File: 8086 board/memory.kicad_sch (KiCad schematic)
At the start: 43 parts, among them U10 74AC573, U11 74HC138, U12 74HC138, U13 IS61C6416AL, U3 74HC14, U39 29F800BA, U40 IS61C6416AL, U8 74AC573, U9 74AC573

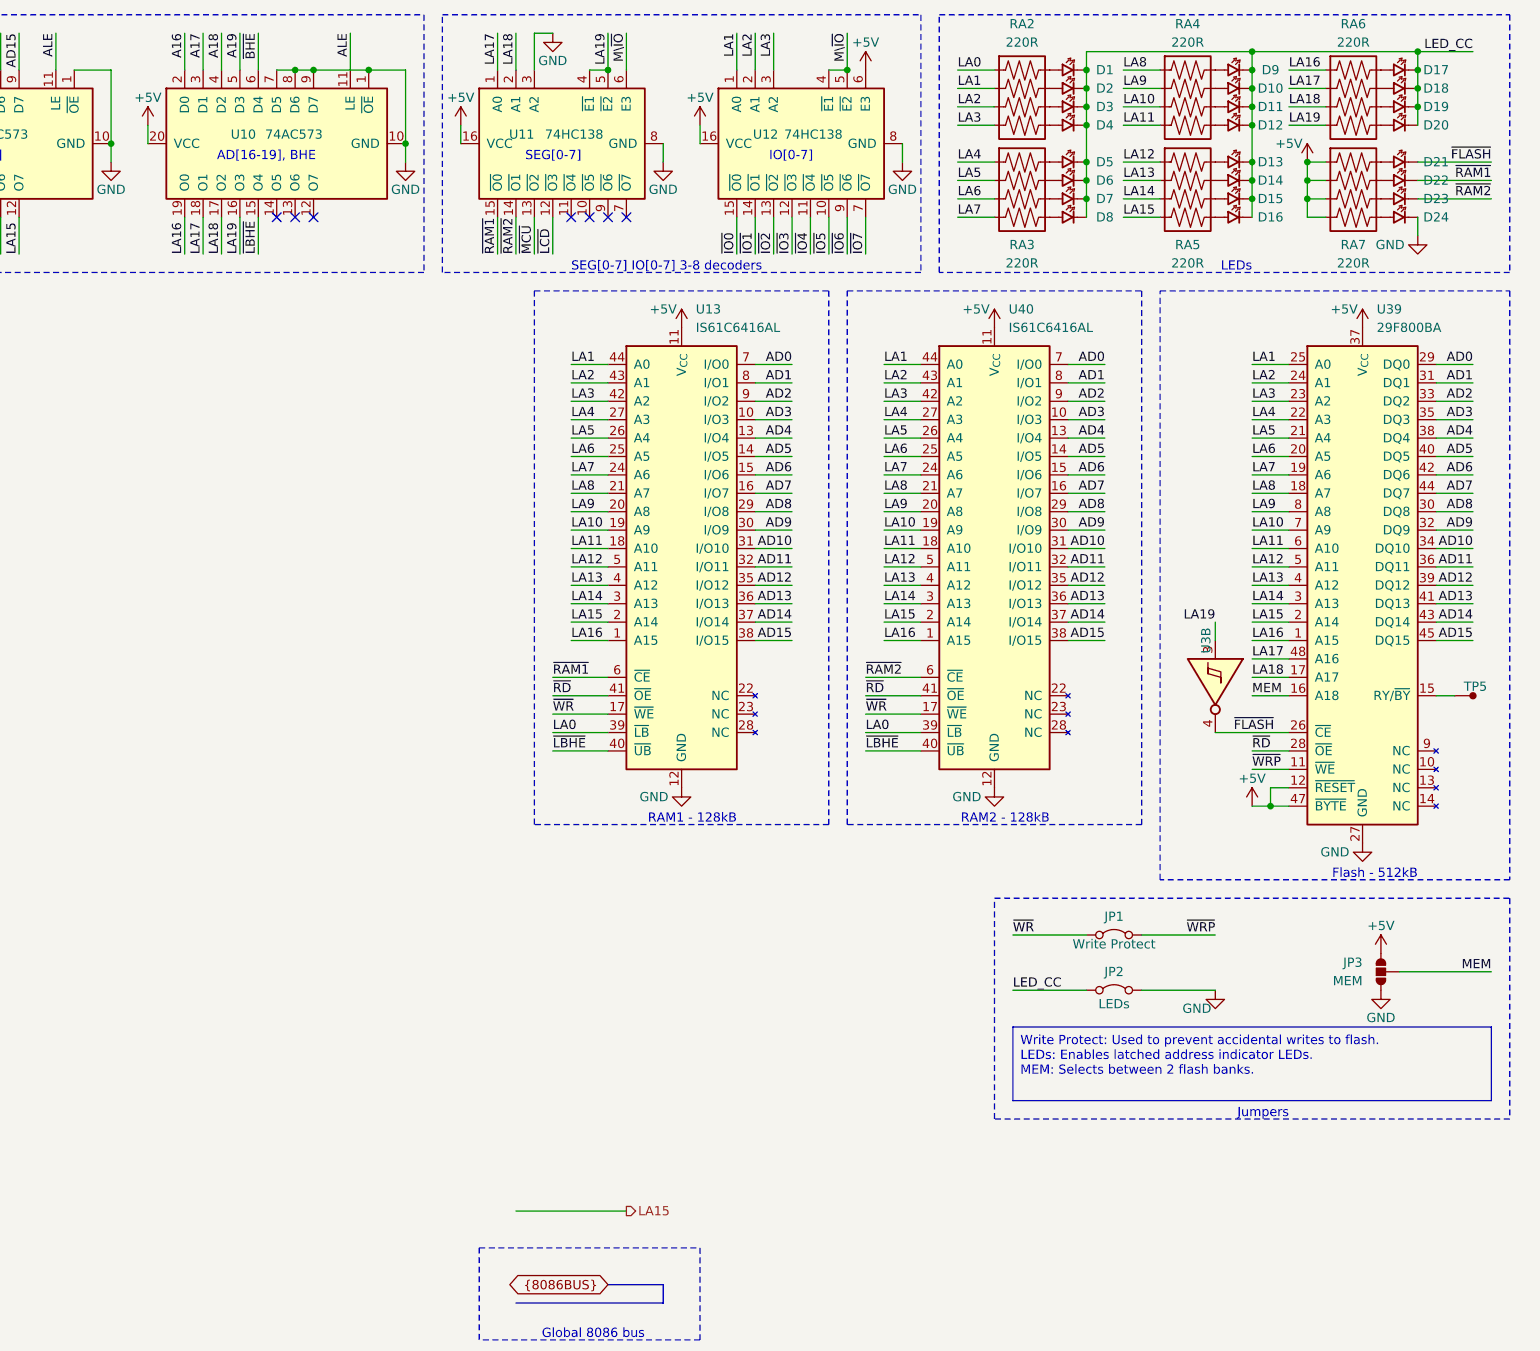
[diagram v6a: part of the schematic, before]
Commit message: reduced schematic, PCB memory routed
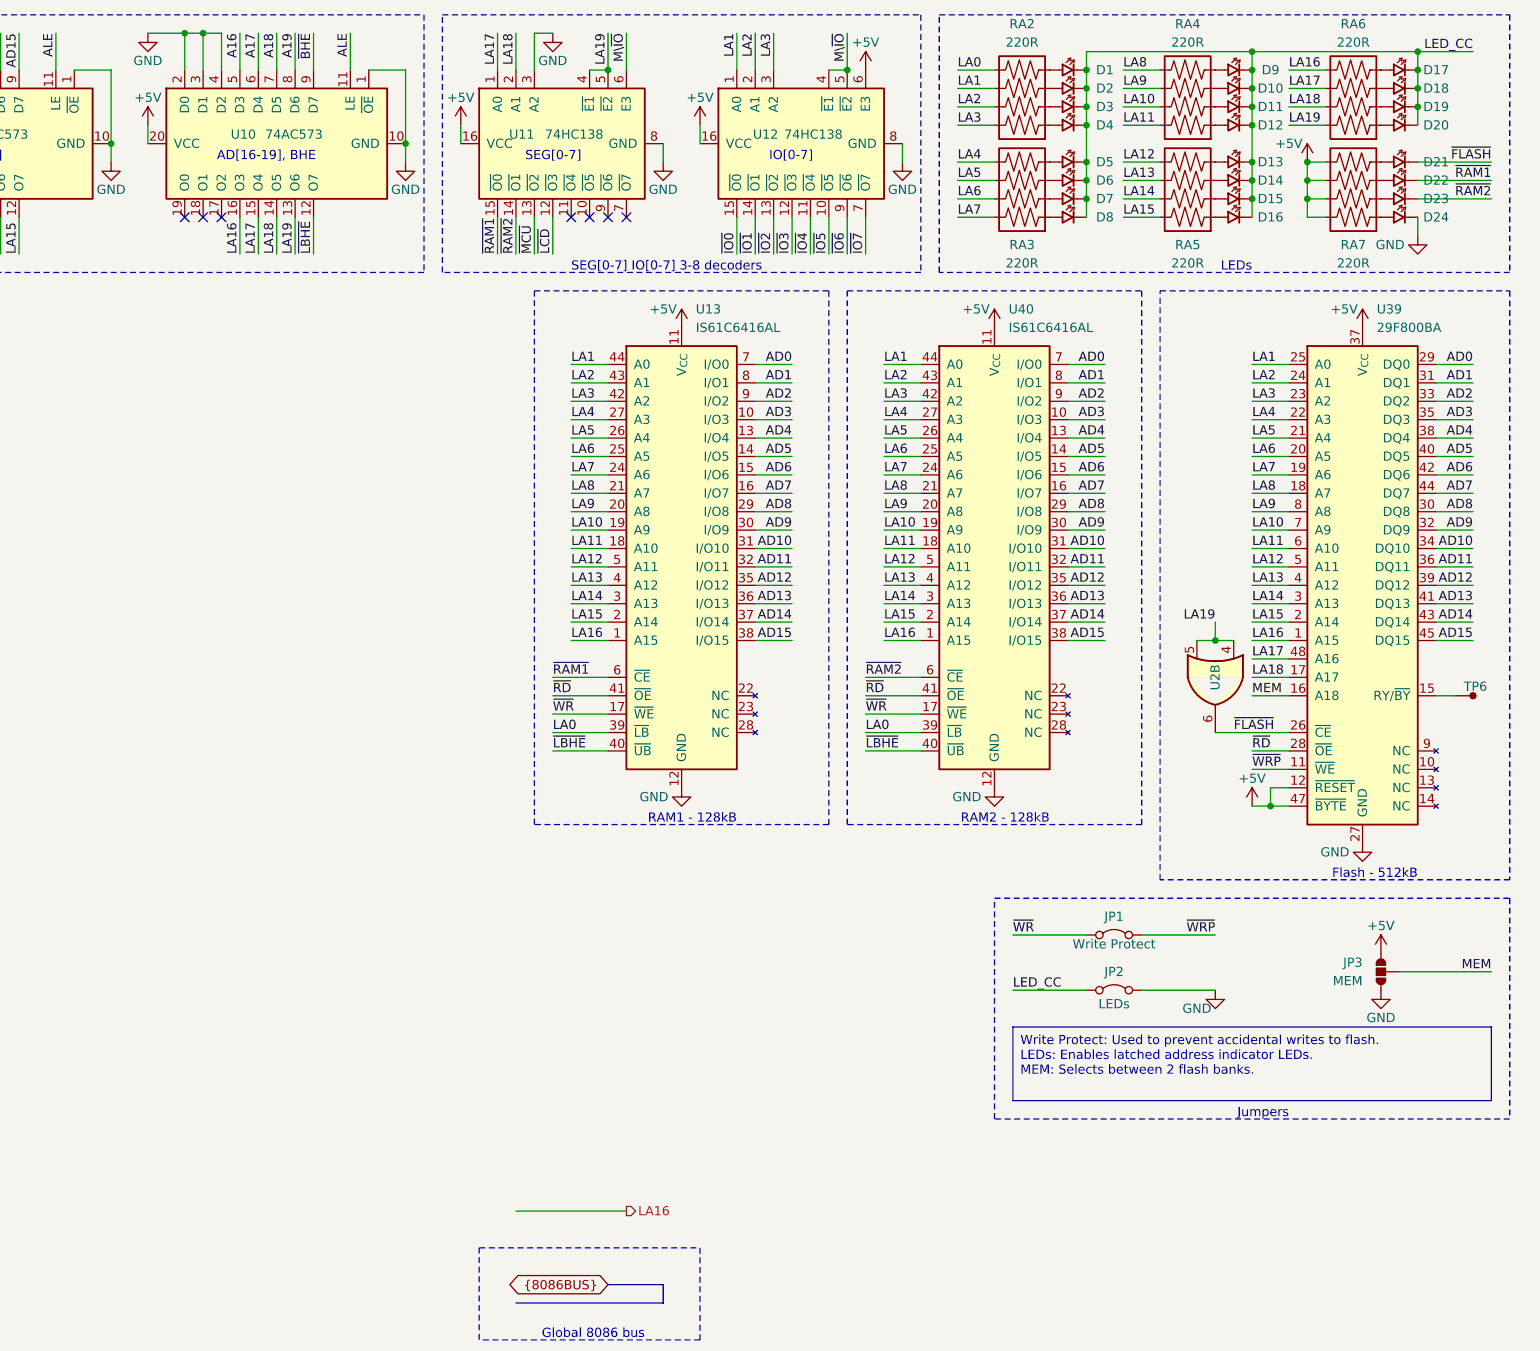
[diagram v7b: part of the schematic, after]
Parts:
- removed U3: 74HC14, Package_SO:SOIC-14_3.9x8.7mm_P1.27mm, symbol 8086PC:74HC14
- added U2: 74HC32, Package_SO:TSSOP-14_4.4x5mm_P0.65mm, symbol 8086PC:74HC32
- D21: value PWR -> FLASH
- D22: value ~{BHE} -> RAM1
- D23: value SEG0 -> RAM2
- D24: value SEG1 -> POWER
- TP6: renamed from TP5; footprint (none) -> TestPoint:TestPoint_Pad_1.5x1.5mm
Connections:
- net +5V: now also JP3.3, RA7.5, RA7.6, RA7.7, RA7.8; no longer JP3.2, RA7.1, RA7.2, RA7.3, RA7.4
- net A16: now also U10.5 (D3); no longer U10.2 (D0)
- net A17: now also U10.6 (D4); no longer U10.3 (D1)
- net A18: now also U10.7 (D5); no longer U10.4 (D2)
- net A19: now also U10.8 (D6); no longer U10.5 (D3)
- net GND: now also U10.2 (D0), U10.3 (D1), U10.4 (D2); no longer U10.7 (D5), U10.8 (D6), U10.9 (D7)
- net LA0: now also RA2.5; no longer RA2.1
- net LA1: now also RA2.6; no longer RA2.2
- net LA10: now also RA4.7; no longer RA4.3
- net LA11: now also RA4.8; no longer RA4.4
- net LA12: now also RA5.5; no longer RA5.1
- net LA13: now also RA5.6; no longer RA5.2
- net LA14: now also RA5.7; no longer RA5.3
- net LA15: now also RA5.8; no longer RA5.4
- net LA16: now also RA6.5, U10.16 (O3); no longer RA6.1, U10.19 (O0)
- net LA17: now also RA6.6, U10.15 (O4); no longer RA6.2, U10.18 (O1)
- net LA18: now also RA6.7, U10.14 (O5); no longer RA6.3, U10.17 (O2)
- net LA19: now also RA6.8, U10.13 (O6), U2.4, U2.5; no longer RA6.4, U10.16 (O3)
- net LA2: now also RA2.7; no longer RA2.3
- net LA3: now also RA2.8; no longer RA2.4
- net LA4: now also RA3.5; no longer RA3.1
- net LA5: now also RA3.6; no longer RA3.2
- net LA6: now also RA3.7; no longer RA3.3
- net LA7: now also RA3.8; no longer RA3.4
- net LA8: now also RA4.5; no longer RA4.1
- net LA9: now also RA4.6; no longer RA4.2
- net MEM: now also JP3.2; no longer JP3.3
- net ~{BHE}: now also U10.9 (D7); no longer U10.6 (D4)
- net ~{FLASH}: now also U2.6
- net ~{LBHE}: now also U10.12 (O7); no longer U10.15 (O4)
- net at D4.1 (A): now also RA2.1; no longer RA2.5
- net at D3.1 (A): now also RA2.2; no longer RA2.6
- net at D2.1 (A): now also RA2.3; no longer RA2.7
- net at D1.1 (A): now also RA2.4; no longer RA2.8
- net at D19.1 (A): now also RA6.2; no longer RA6.6
- net at D23.1 (A): now also RA7.2; no longer RA7.6
- net at D8.1 (A): now also RA3.1; no longer RA3.5
- net at D21.1 (A): now also RA7.4; no longer RA7.8
- net at D22.1 (A): now also RA7.3; no longer RA7.7
- net at D20.1 (A): now also RA6.1; no longer RA6.5
- net at D12.1 (A): now also RA4.1; no longer RA4.5
- net at D7.1 (A): now also RA3.2; no longer RA3.6
- net at D6.1 (A): now also RA3.3; no longer RA3.7
- net at D5.1 (A): now also RA3.4; no longer RA3.8
- net at D18.1 (A): now also RA6.3; no longer RA6.7
- net at D17.1 (A): now also RA6.4; no longer RA6.8
- net at D15.1 (A): now also RA5.2; no longer RA5.6
- net at D11.1 (A): now also RA4.2; no longer RA4.6
- net at D10.1 (A): now also RA4.3; no longer RA4.7
- net at D16.1 (A): now also RA5.1; no longer RA5.5
- net at D14.1 (A): now also RA5.3; no longer RA5.7
- net at D13.1 (A): now also RA5.4; no longer RA5.8
- net at D9.1 (A): now also RA4.4; no longer RA4.8
- net at D24.1 (A): now also RA7.1; no longer RA7.5
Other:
- moved on the sheet: RA2, RA3, RA4, RA5, RA6, RA7

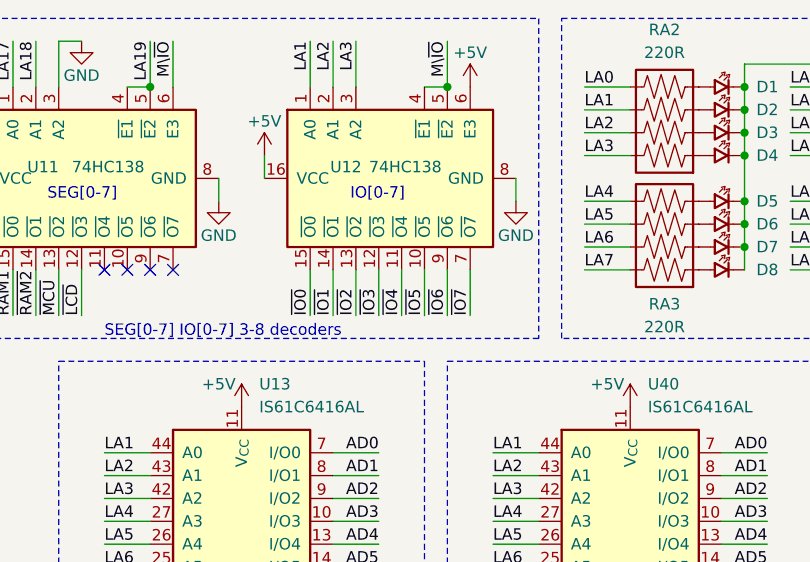
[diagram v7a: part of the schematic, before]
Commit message: schematic: reduced 8086 bus, no LCD shield
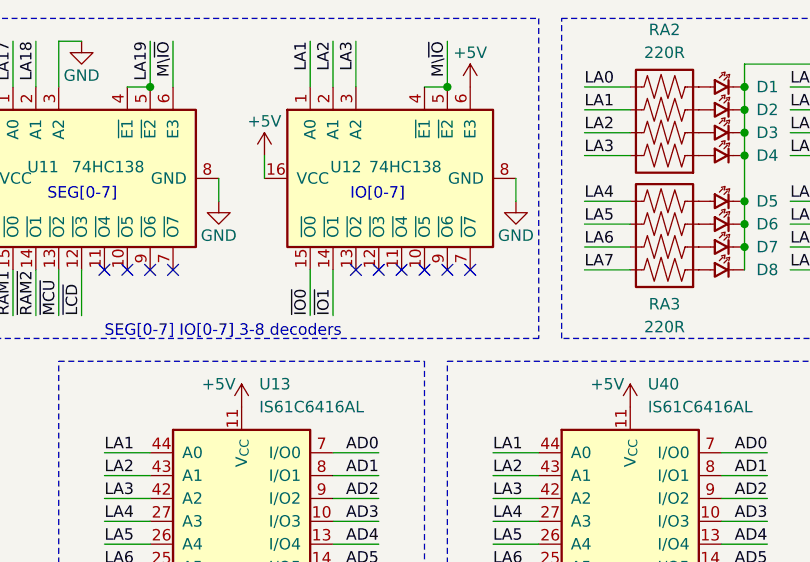
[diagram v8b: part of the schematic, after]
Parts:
- U11, U12: footprint Package_SO:SOIC-16_3.9x9.9mm_P1.27mm -> Package_SO:TSSOP-16_4.4x5mm_P0.65mm
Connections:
- net ~{IO2}: no longer names the net of U12.13 (~{O2})
- net ~{IO3}: no longer names the net of U12.12 (~{O3})
- net ~{IO4}: no longer names the net of U12.11 (~{O4})
- net ~{IO5}: no longer names the net of U12.10 (~{O5})
- net ~{IO6}: no longer names the net of U12.9 (~{O6})
- net ~{IO7}: no longer names the net of U12.7 (~{O7})
- no-connect marks 7 -> 13
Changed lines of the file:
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@@
   )
   (no_connect (at 154.94 40.64))
+  (no_connect (at 182.88 40.64))
+  (no_connect (at 185.42 40.64))
   (no_connect (at 162.56 40.64))
+  (no_connect (at 193.04 40.64))
   (no_connect (at 157.48 40.64))
   (no_connect (at 106.68 40.64))
   (no_connect (at 160.02 40.64))
+  (no_connect (at 195.58 40.64))
   (no_connect (at 101.6 40.64))
+  (no_connect (at 190.5 40.64))
   (no_connect (at 104.14 40.64))
+  (no_connect (at 187.96 40.64))
   (wire (pts (xy 109.22 15.24) (xy 109.22 20.32))
     (stroke (width 0) (type default))
@@
     (stroke (width 0) (type default))
   )
-  (wire (pts (xy 187.96 40.64) (xy 187.96 45.72))
-    (stroke (width 0) (type default))
-  )
   (wire (pts (xy 228.6 71.12) (xy 223.52 71.12))
     (stroke (width 0) (type default))
@@
     (stroke (width 0) (type default))
   )
-  (wire (pts (xy 182.88 40.64) (xy 182.88 45.72))
-    (stroke (width 0) (type default))
-  )
   (wire (pts (xy 154.94 88.9) (xy 160.02 88.9))
     (stroke (width 0) (type default))
@@
     (stroke (width 0) (type default))
   )
-  (wire (pts (xy 195.58 40.64) (xy 195.58 45.72))
-    (stroke (width 0) (type default))
-  )
   (wire (pts (xy 185.42 78.74) (xy 180.34 78.74))
     (stroke (width 0) (type default))
@@
     (stroke (width 0) (type default))
   )
-  (wire (pts (xy 185.42 40.64) (xy 185.42 45.72))
-    (stroke (width 0) (type default))
-  )
   (wire (pts (xy 111.76 40.64) (xy 111.76 45.72))
     (stroke (width 0) (type default))
@@
     (stroke (width 0) (type default))
   )
-  (wire (pts (xy 193.04 40.64) (xy 193.04 45.72))
-    (stroke (width 0) (type default))
-  )
   (wire (pts (xy 185.42 73.66) (xy 180.34 73.66))
     (stroke (width 0) (type default))
@@
     (stroke (width 0) (type default))
   )
-  (wire (pts (xy 190.5 40.64) (xy 190.5 45.72))
-    (stroke (width 0) (type default))
-  )
   (wire (pts (xy 20.32 40.64) (xy 20.32 45.72))
     (stroke (width 0) (type default))
@@
     (effects (font (size 1.27 1.27)) (justify left bottom))
   )
-  (label "~{IO4}" (at 187.96 45.72 90) (fields_autoplaced)
-    (effects (font (size 1.27 1.27)) (justify left bottom))
-  )
   (label "LA8" (at 60.96 45.72 90) (fields_autoplaced)
     (effects (font (size 1.27 1.27)) (justify left bottom))
@@
     (effects (font (size 1.27 1.27)) (justify right bottom))
   )
-  (label "~{IO7}" (at 195.58 45.72 90) (fields_autoplaced)
-    (effects (font (size 1.27 1.27)) (justify left bottom))
-  )
   (label "AD7" (at 279.4 78.74 180) (fields_autoplaced)
     (effects (font (size 1.27 1.27)) (justify right bottom))
@@
     (effects (font (size 1.27 1.27)) (justify right bottom))
   )
-  (label "~{IO5}" (at 190.5 45.72 90) (fields_autoplaced)
-    (effects (font (size 1.27 1.27)) (justify left bottom))
-  )
   (label "LA16" (at 154.94 99.06 0) (fields_autoplaced)
     (effects (font (size 1.27 1.27)) (justify left bottom))
@@
     (effects (font (size 1.27 1.27)) (justify right bottom))
   )
-  (label "~{IO3}" (at 185.42 45.72 90) (fields_autoplaced)
-    (effects (font (size 1.27 1.27)) (justify left bottom))
-  )
   (label "AD14" (at 228.6 96.52 180) (fields_autoplaced)
     (effects (font (size 1.27 1.27)) (justify right bottom))
@@
     (effects (font (size 1.27 1.27)) (justify right bottom))
   )
-  (label "~{IO2}" (at 182.88 45.72 90) (fields_autoplaced)
-    (effects (font (size 1.27 1.27)) (justify left bottom))
-  )
   (label "AD11" (at 279.4 88.9 180) (fields_autoplaced)
     (effects (font (size 1.27 1.27)) (justify right bottom))
@@
     (effects (font (size 1.27 1.27)) (justify right bottom))
   )
-  (label "~{IO6}" (at 193.04 45.72 90) (fields_autoplaced)
-    (effects (font (size 1.27 1.27)) (justify left bottom))
-  )
   (global_label "{8086BUS}" (shape bidirectional) (at 160.02 187.96 180) (fields_autoplaced)
     (effects (font (size 1.27 1.27)) (justify right))
@@
   )
   (symbol (lib_id "8086PC:74HC32") (at 243.84 104.14 270) (unit 2)
-    (in_bom no) (on_board no) (dnp no)
+    (in_bom no) (on_board yes) (dnp no)
     (property "Reference" "U2" (at 243.84 104.14 0)
       (effects (font (size 1.27 1.27)))
@@
       (effects (font (size 1.27 1.27)) (justify left))
     )
-    (property "Footprint" "Package_SO:SOIC-16_3.9x9.9mm_P1.27mm" (at 152.4 30.48 0)
+    (property "Footprint" "Package_SO:TSSOP-16_4.4x5mm_P0.65mm" (at 152.4 30.48 0)
       (effects (font (size 1.27 1.27)) hide)
     )
@@
       (effects (font (size 1.27 1.27)) (justify left))
     )
-    (property "Footprint" "Package_SO:SOIC-16_3.9x9.9mm_P1.27mm" (at 185.42 30.48 0)
+    (property "Footprint" "Package_SO:TSSOP-16_4.4x5mm_P0.65mm" (at 185.42 30.48 0)
       (effects (font (size 1.27 1.27)) hide)
     )
